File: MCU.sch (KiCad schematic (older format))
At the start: 0 parts

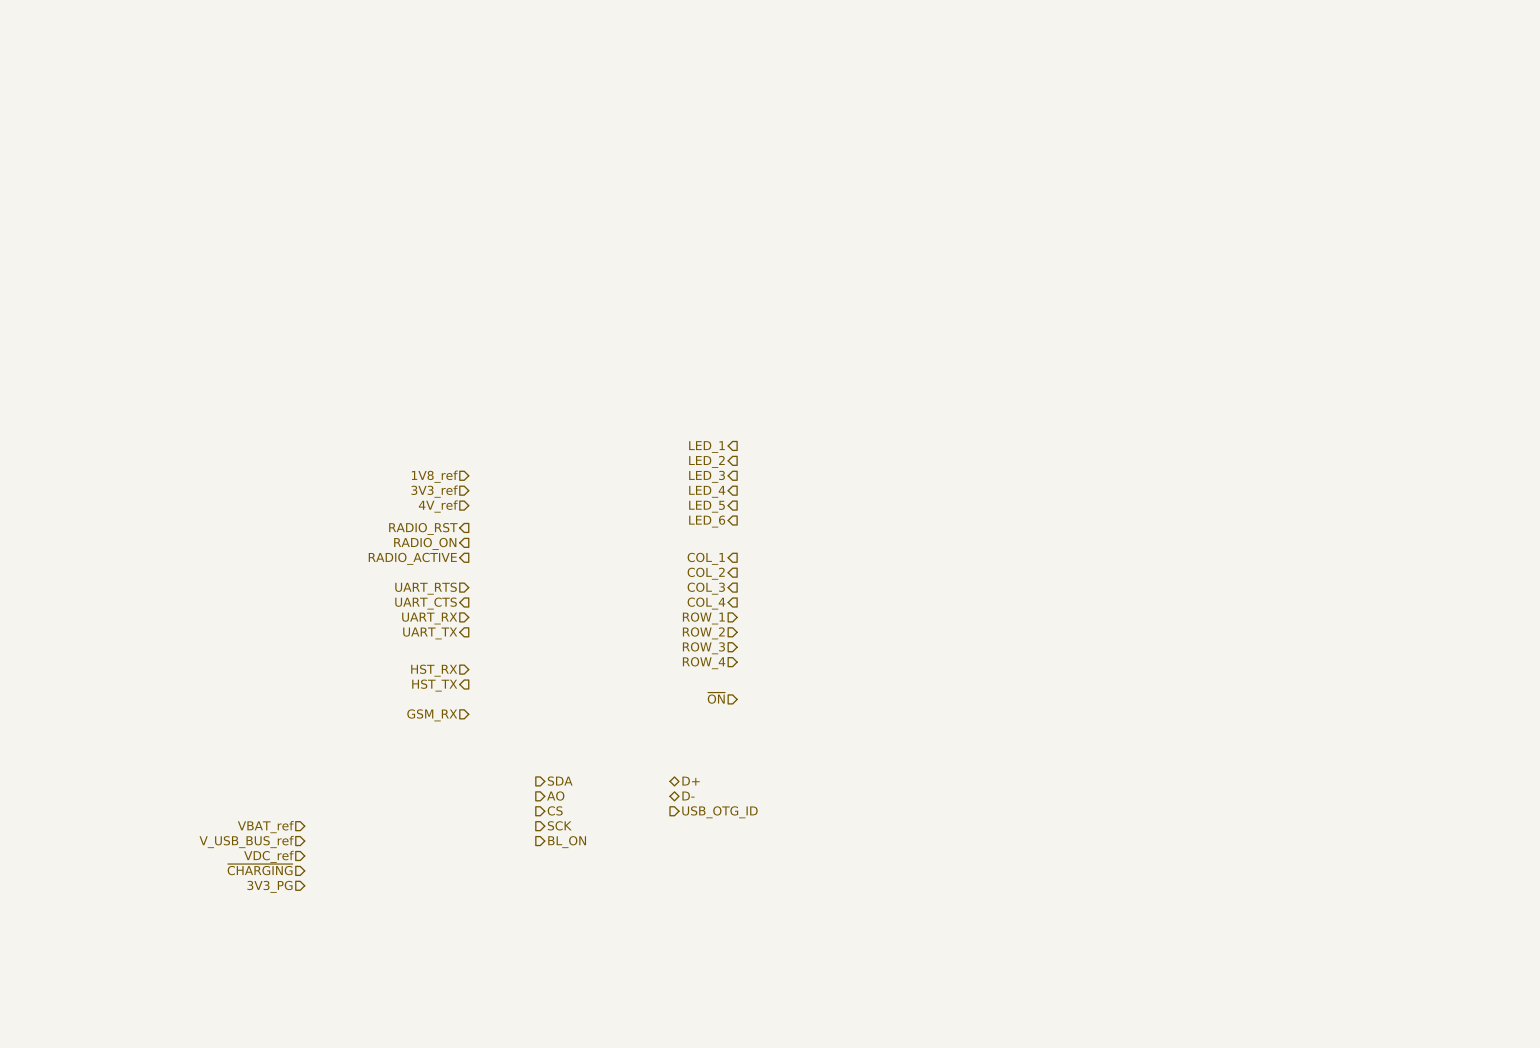
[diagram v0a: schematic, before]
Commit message: Schematics:  - Added STZM32 MCU for the CPU kernel  - Added ESP8266 for WiFi Subsheet
Firmware:
 - Generated BIOS configuration for CubeMX
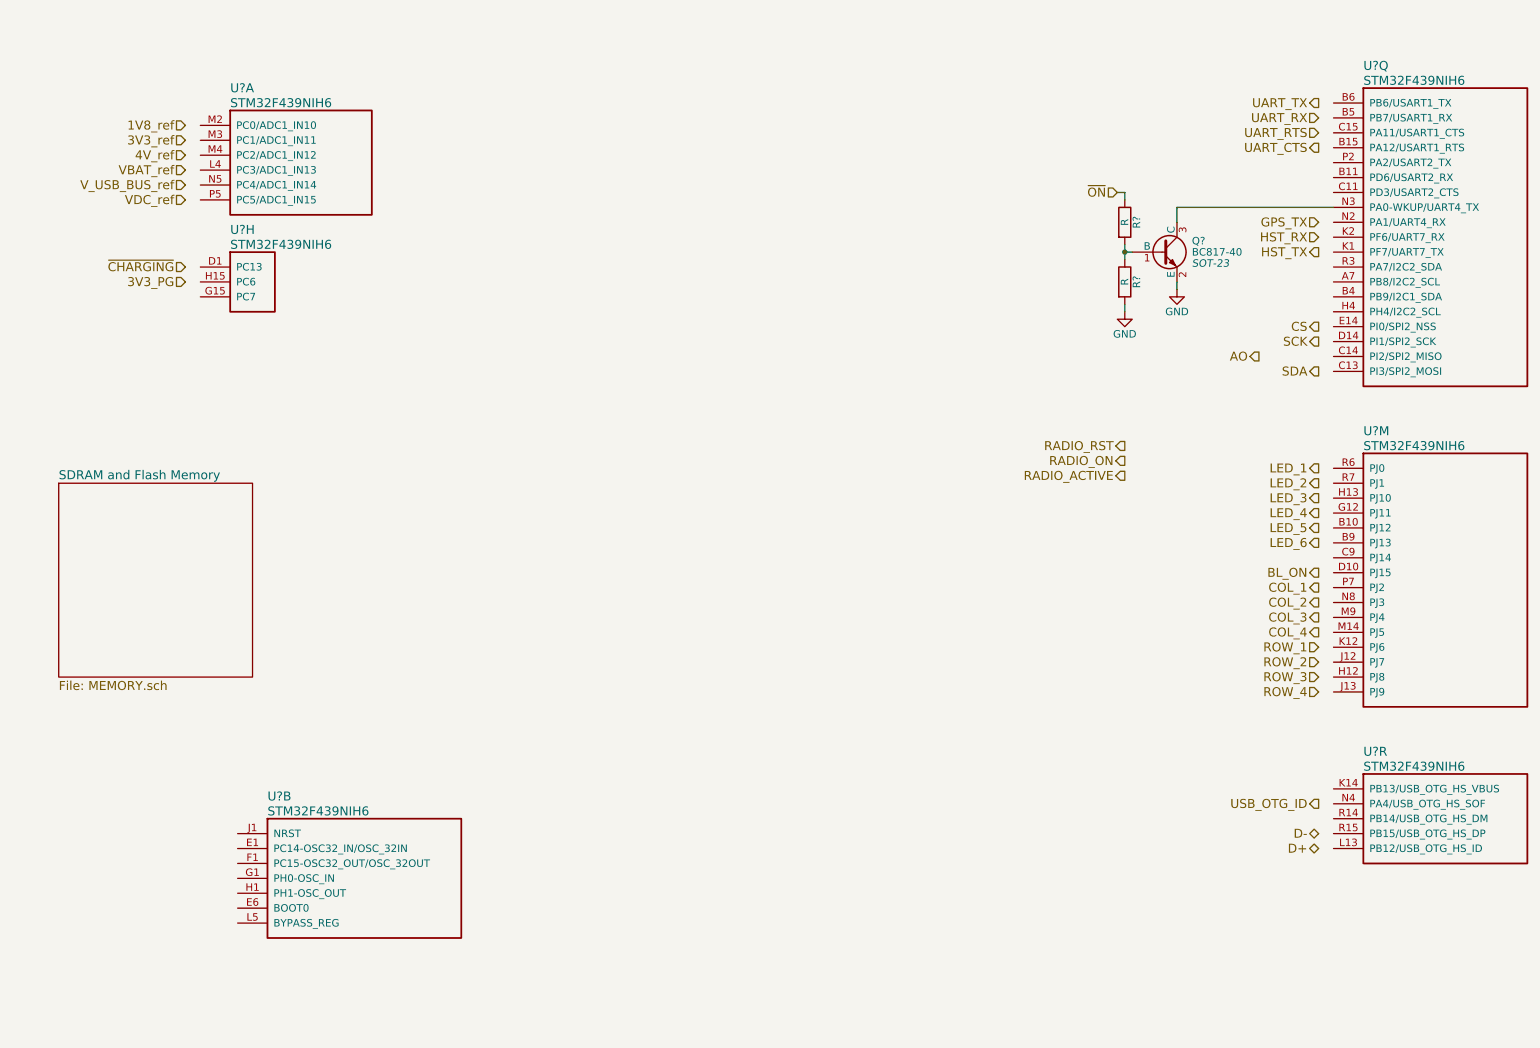
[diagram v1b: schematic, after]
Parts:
- added Q?: BC817-40, SOT-23, symbol BC817-40
- added R? (x2): R, symbol R
- added U? (x6): STM32F439NIH6, symbol STM32F439NIH6
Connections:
- net ~ON: now also R?.1
- new net: Q?.3 (C), U?.N3 (PA0-WKUP/UART4_TX)
- new net: Q?.1 (B), R?.1, R?.2
- new net GND: Q?.2 (E), R?.2
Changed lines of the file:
@@
 LIBS:tps61045
 LIBS:tps62172
+LIBS:mma8451q
+LIBS:STM32F439NIH6
 LIBS:3310retro-cache
 EELAYER 25 0
@@
 $Descr A4 11693 8268
 encoding utf-8
-Sheet 2 7
-Title "Nokia 3210 Retrofit"
-Date "2016-10-18"
+Sheet 2 9
+Title "Nokia 3310 Retrofit"
+Date "2016-10-23"
 Rev "1"
 Comp ""
@@
 Comment4 ""
 $EndDescr
-Text HLabel 5750 3550 0    60   Output ~ 0
+Text HLabel 9650 3700 0    60   Output ~ 0
 LED_1
-Text HLabel 5750 3650 0    60   Output ~ 0
+Text HLabel 9650 3800 0    60   Output ~ 0
 LED_2
-Text HLabel 5750 3750 0    60   Output ~ 0
+Text HLabel 9650 3900 0    60   Output ~ 0
 LED_3
-Text HLabel 5750 3850 0    60   Output ~ 0
+Text HLabel 9650 4000 0    60   Output ~ 0
 LED_4
-Text HLabel 5750 3950 0    60   Output ~ 0
+Text HLabel 9650 4100 0    60   Output ~ 0
 LED_5
-Text HLabel 5750 4050 0    60   Output ~ 0
+Text HLabel 9650 4200 0    60   Output ~ 0
 LED_6
-Text HLabel 5750 4300 0    60   Output ~ 0
+Text HLabel 9650 4500 0    60   Output ~ 0
 COL_1
-Text HLabel 5750 4400 0    60   Output ~ 0
+Text HLabel 9650 4600 0    60   Output ~ 0
 COL_2
-Text HLabel 5750 4500 0    60   Output ~ 0
+Text HLabel 9650 4700 0    60   Output ~ 0
 COL_3
-Text HLabel 5750 4600 0    60   Output ~ 0
+Text HLabel 9650 4800 0    60   Output ~ 0
 COL_4
-Text HLabel 5750 4700 0    60   Input ~ 0
+Text HLabel 9650 4900 0    60   Input ~ 0
 ROW_1
-Text HLabel 5750 4800 0    60   Input ~ 0
+Text HLabel 9650 5000 0    60   Input ~ 0
 ROW_2
-Text HLabel 5750 4900 0    60   Input ~ 0
+Text HLabel 9650 5100 0    60   Input ~ 0
 ROW_3
-Text HLabel 5750 5000 0    60   Input ~ 0
+Text HLabel 9650 5200 0    60   Input ~ 0
 ROW_4
-Text HLabel 5750 5250 0    60   Input ~ 0
+Text HLabel 8300 1850 0    60   Input ~ 0
 ~ON
-Text HLabel 3950 3750 0    60   Input ~ 0
+Text HLabel 2050 1400 0    60   Input ~ 0
 1V8_ref
-Text HLabel 3950 3850 0    60   Input ~ 0
+Text HLabel 2050 1500 0    60   Input ~ 0
 3V3_ref
-Text HLabel 3950 3950 0    60   Input ~ 0
+Text HLabel 2050 1600 0    60   Input ~ 0
 4V_ref
-Text HLabel 3950 4100 0    60   Output ~ 0
+Text HLabel 8350 3550 0    60   Output ~ 0
 RADIO_RST
-Text HLabel 3950 4200 0    60   Output ~ 0
+Text HLabel 8350 3650 0    60   Output ~ 0
 RADIO_ON
-Text HLabel 3950 4300 0    60   Output ~ 0
+Text HLabel 8350 3750 0    60   Output ~ 0
 RADIO_ACTIVE
-Text HLabel 3950 4500 0    60   Input ~ 0
+Text HLabel 9650 1450 0    60   Input ~ 0
 UART_RTS
-Text HLabel 3950 4600 0    60   Output ~ 0
+Text HLabel 9650 1550 0    60   Output ~ 0
 UART_CTS
-Text HLabel 3950 4700 0    60   Input ~ 0
+Text HLabel 9650 1350 0    60   Input ~ 0
 UART_RX
-Text HLabel 3950 4800 0    60   Output ~ 0
+Text HLabel 9650 1250 0    60   Output ~ 0
 UART_TX
-Text HLabel 3950 5050 0    60   Input ~ 0
+Text HLabel 9650 2150 0    60   Input ~ 0
 HST_RX
-Text HLabel 3950 5150 0    60   Output ~ 0
+Text HLabel 9650 2250 0    60   Output ~ 0
 HST_TX
-Text HLabel 3950 5350 0    60   Input ~ 0
-GSM_RX
-Text HLabel 4400 5800 2    60   Output ~ 0
+Text HLabel 9650 3050 0    60   Output ~ 0
 SDA
-Text HLabel 4400 5900 2    60   Output ~ 0
+Text HLabel 9250 2950 0    60   Output ~ 0
 AO
-Text HLabel 4400 6000 2    60   Output ~ 0
+Text HLabel 9650 2750 0    60   Output ~ 0
 CS
-Text HLabel 4400 6100 2    60   Output ~ 0
+Text HLabel 9650 2850 0    60   Output ~ 0
 SCK
-Text HLabel 4400 6200 2    60   Output ~ 0
+Text HLabel 9650 4400 0    60   Output ~ 0
 BL_ON
-Text HLabel 5300 5800 2    60   BiDi ~ 0
+Text HLabel 9650 6250 0    60   BiDi ~ 0
 D+
-Text HLabel 5300 5900 2    60   BiDi ~ 0
+Text HLabel 9650 6150 0    60   BiDi ~ 0
 D-
-Text HLabel 5300 6000 2    60   Output ~ 0
+Text HLabel 9650 5950 0    60   Output ~ 0
 USB_OTG_ID
-Text HLabel 2850 6100 0    60   Input ~ 0
+Text HLabel 2050 1700 0    60   Input ~ 0
 VBAT_ref
-Text HLabel 2850 6200 0    60   Input ~ 0
+Text HLabel 2050 1800 0    60   Input ~ 0
 V_USB_BUS_ref
-Text HLabel 2850 6300 0    60   Input ~ 0
+Text HLabel 2050 1900 0    60   Input ~ 0
 VDC_ref
-Text HLabel 2850 6400 0    60   Input ~ 0
+Text HLabel 2050 2350 0    60   Input ~ 0
 ~CHARGING
-Text HLabel 2850 6500 0    60   Input ~ 0
+Text HLabel 2050 2450 0    60   Input ~ 0
 3V3_PG
+$Comp
+L STM32F439NIH6 U?
+U 1 1 580D4E7A
+P 2150 1400
+F 0 "U?" H 2350 1650 60  0000 L CNN
+F 1 "STM32F439NIH6" H 2350 1550 60  0000 L CNN
+F 2 "" H 2150 1400 60  0000 C CNN
+F 3 "" H 2150 1400 60  0000 C CNN
+	1    2150 1400
+	1    0    0    -1
+$EndComp
+$Comp
+L STM32F439NIH6 U?
+U 8 1 580D4EF2
+P 2150 2350
+F 0 "U?" H 2350 2600 60  0000 L CNN
+F 1 "STM32F439NIH6" H 2350 2500 60  0000 L CNN
+F 2 "" H 2150 2350 60  0000 C CNN
+F 3 "" H 2150 2350 60  0000 C CNN
+	8    2150 2350
+	1    0    0    -1
+$EndComp
+$Comp
+L STM32F439NIH6 U?
+U 13 1 580D9CC6
+P 9750 3700
+F 0 "U?" H 9950 3950 60  0000 L CNN
+F 1 "STM32F439NIH6" H 9950 3850 60  0000 L CNN
+F 2 "" H 9750 3700 60  0000 C CNN
+F 3 "" H 9750 3700 60  0000 C CNN
+	13   9750 3700
+	1    0    0    -1
+$EndComp
+$Comp
+L STM32F439NIH6 U?
+U 2 1 580D9DC1
+P 2400 6150
+F 0 "U?" H 2600 6400 60  0000 L CNN
+F 1 "STM32F439NIH6" H 2600 6300 60  0000 L CNN
+F 2 "" H 2400 6150 60  0000 C CNN
+F 3 "" H 2400 6150 60  0000 C CNN
+	2    2400 6150
+	1    0    0    -1
+$EndComp
+$Comp
+L STM32F439NIH6 U?
+U 17 1 580D9E16
+P 9750 1250
+F 0 "U?" H 9950 1500 60  0000 L CNN
+F 1 "STM32F439NIH6" H 9950 1400 60  0000 L CNN
+F 2 "" H 9750 1250 60  0000 C CNN
+F 3 "" H 9750 1250 60  0000 C CNN
+	17   9750 1250
+	1    0    0    -1
+$EndComp
+$Sheet
+S 1200 3800 1300 1300
+U 580D9E7F
+F0 "SDRAM and Flash Memory" 60
+F1 "MEMORY.sch" 60
+$EndSheet
+$Comp
+L STM32F439NIH6 U?
+U 18 1 580D9EED
+P 9750 5850
+F 0 "U?" H 9950 6100 60  0000 L CNN
+F 1 "STM32F439NIH6" H 9950 6000 60  0000 L CNN
+F 2 "" H 9750 5850 60  0000 C CNN
+F 3 "" H 9750 5850 60  0000 C CNN
+	18   9750 5850
+	1    0    0    -1
+$EndComp
+Text HLabel 9650 2050 0    60   Input ~ 0
+GPS_TX
+$Comp
+L BC817-40 Q?
+U 1 1 580DD654
+P 8600 2250
+F 0 "Q?" H 8800 2325 50  0000 L CNN
+F 1 "BC817-40" H 8800 2250 50  0000 L CNN
+F 2 "SOT-23" H 8800 2175 50  0000 L CIN
+F 3 "" H 8600 2250 50  0000 L CNN
+	1    8600 2250
+	1    0    0    -1
+$EndComp
+Wire Wire Line
+	9750 1950 8700 1950
+Wire Wire Line
+	8700 1950 8700 2050
+$Comp
+L GND #PWR?
+U 1 1 580DD6FB
+P 8700 2500
+F 0 "#PWR?" H 8700 2250 50  0001 C CNN
+F 1 "GND" H 8700 2350 50  0000 C CNN
+F 2 "" H 8700 2500 50  0000 C CNN
+F 3 "" H 8700 2500 50  0000 C CNN
+	1    8700 2500
+	1    0    0    -1
+$EndComp
+Wire Wire Line
+	8700 2500 8700 2450
+$Comp
+L R R?
+U 1 1 580DD728
+P 8350 2450
+F 0 "R?" V 8430 2450 50  0000 C CNN
+F 1 "R" V 8350 2450 50  0000 C CNN
+F 2 "" V 8280 2450 50  0000 C CNN
+F 3 "" H 8350 2450 50  0000 C CNN
+	1    8350 2450
+	1    0    0    -1
+$EndComp
+$Comp
+L R R?
+U 1 1 580DD7A3
+P 8350 2050
+F 0 "R?" V 8430 2050 50  0000 C CNN
+F 1 "R" V 8350 2050 50  0000 C CNN
+F 2 "" V 8280 2050 50  0000 C CNN
+F 3 "" H 8350 2050 50  0000 C CNN
+	1    8350 2050
+	1    0    0    -1
+$EndComp
+Wire Wire Line
+	8350 2200 8350 2300
+Wire Wire Line
+	8400 2250 8350 2250
+Connection ~ 8350 2250
+Wire Wire Line
+	8300 1850 8350 1850
+Wire Wire Line
+	8350 1850 8350 1900
+$Comp
+L GND #PWR?
+U 1 1 580DD838
+P 8350 2650
+F 0 "#PWR?" H 8350 2400 50  0001 C CNN
+F 1 "GND" H 8350 2500 50  0000 C CNN
+F 2 "" H 8350 2650 50  0000 C CNN
+F 3 "" H 8350 2650 50  0000 C CNN
+	1    8350 2650
+	1    0    0    -1
+$EndComp
+Wire Wire Line
+	8350 2650 8350 2600
 $EndSCHEMATC
